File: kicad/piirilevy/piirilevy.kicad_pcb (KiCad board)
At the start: 2 copper layers, 57 parts, among them SW1 SW_SPST, SW2 SW_Push, SW3 SW_Push, SW4 SW_Push, U1 LM324, U2 uA7805, U3 ATmega328P, U4 MAX5033B, U5 MCP3202, U6 47C16, Y1 16MHz

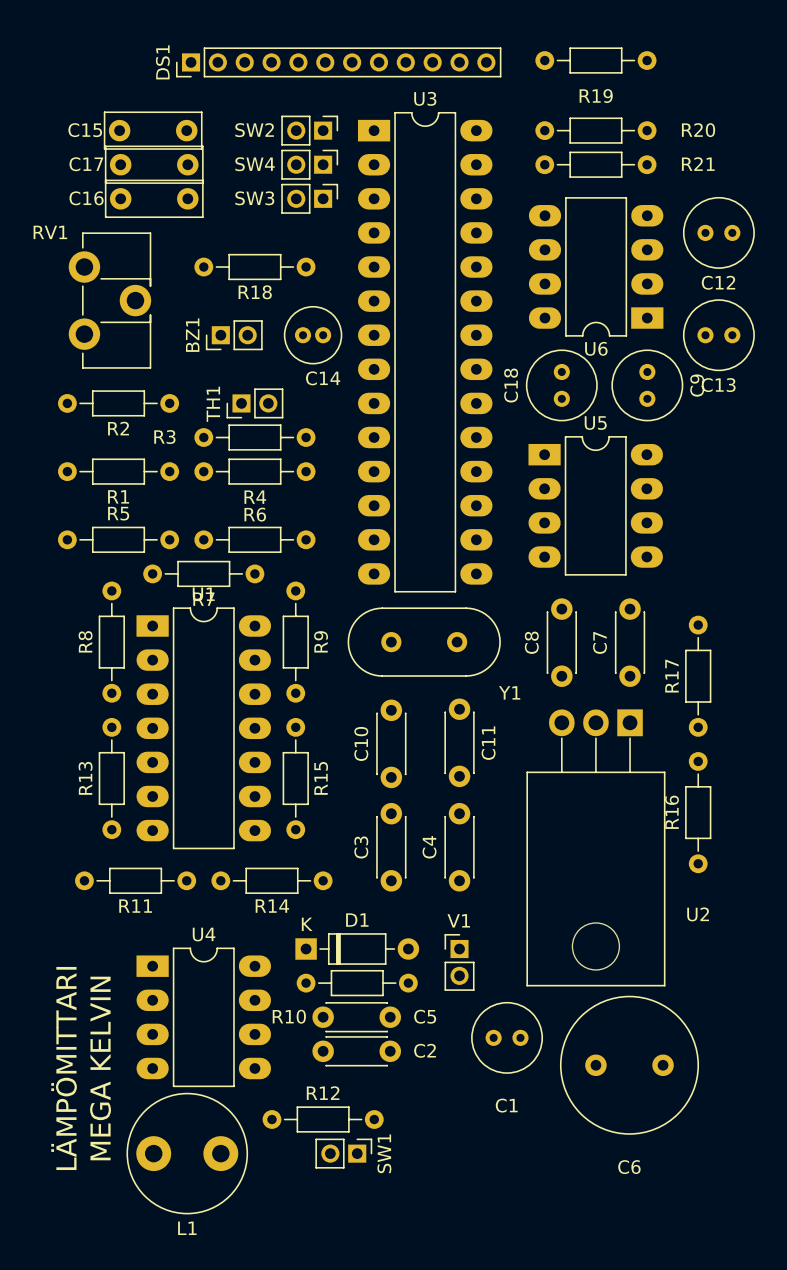
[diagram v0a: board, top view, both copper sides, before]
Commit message: Testausreititys piirilevylle.
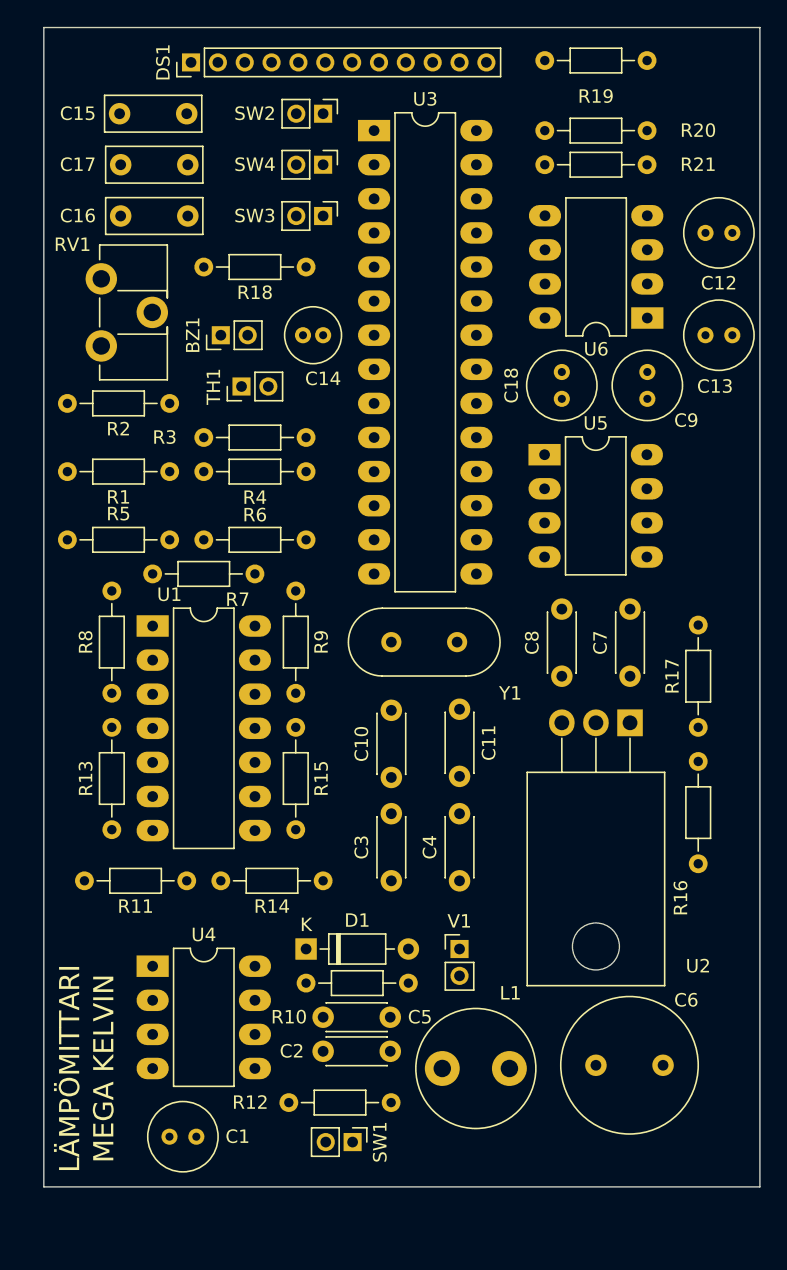
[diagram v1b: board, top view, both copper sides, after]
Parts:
- moved C1 25.2 mm to (121.9, 114.3)
- moved L1 17.7 mm to (142.2, 109.2), turned to 0 degrees
- moved R12 1.78 mm to (130.8, 111.8)
- moved RV1 1.53 mm to (116.8, 50.4)
- moved C16 1.28 mm to (118.3, 45.7)
- moved SW3 1.28 mm to (133.4, 45.7)
- moved C15 1.26 mm to (118.2, 38.1)
- moved SW2 1.26 mm to (133.4, 38.1)
- moved TH1 1.26 mm to (127.3, 58.4)
- moved SW1 0.93 mm to (135.6, 114.7)
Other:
- board outline added: 53.3 x 86.4 mm

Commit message: kicad muutokset
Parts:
- added D2: 1N4148, Diode_THT:D_DO-35_SOD27_P7.62mm_Horizontal, F.Cu at (160.0, 52.1)
- added H1: MountingHole_2.1mm, MountingHole:MountingHole_2.1mm, F.Cu at (114.3, 25.4)
- added H2: MountingHole_2.1mm, MountingHole:MountingHole_2.1mm, F.Cu at (162.6, 25.4)
- added H3: MountingHole_2.1mm, MountingHole:MountingHole_2.1mm, F.Cu at (162.6, 116.8)
- added H4: MountingHole_2.1mm, MountingHole:MountingHole_2.1mm, F.Cu at (114.3, 116.8)
- added J1: AVR-ISP, Connector_PinHeader_2.54mm:PinHeader_2x03_P2.54mm_Vertical, F.Cu at (154.9, 55.9)
- BZ1, SW1, SW2, SW3, SW4, TH1: footprint Connector_PinHeader_2.00mm:PinHeader_1x02_P2.00mm_Vertical -> Connector_PinHeader_2.54mm:PinHeader_1x02_P2.54mm_Vertical
- DS1: footprint Connector_PinHeader_2.00mm:PinHeader_1x12_P2.00mm_Vertical -> Connector_PinHeader_2.54mm:PinHeader_1x12_P2.54mm_Vertical
- RV1: footprint Potentiometer_THT:Potentiometer_ACP_CA9-H3,8_Horizontal -> Potentiometer_THT:Potentiometer_ACP_CA6-H2,5_Horizontal
- moved R19 40.8 mm to (116.8, 30.5), turned to 0 degrees
- moved R20 30.5 mm to (128.3, 30.5), turned to 0 degrees
- moved C13 24.7 mm to (158.4, 30.5)
- moved C12 20.1 mm to (152.4, 30.5)
- moved C5 16.6 mm to (116.8, 104.1), turned to 90 degrees
- moved C2 16.6 mm to (116.8, 106.7), turned to -90 degrees
- moved R21 16.2 mm to (146.1, 30.5)
- moved C1 13.8 mm to (133.6, 106.9)
- moved R12 10.2 mm to (120.7, 111.8)
- moved C9 9.29 mm to (155.5, 48.3)
- moved C18 9.17 mm to (149.9, 48.3)
- moved U6 8.97 mm to (158.8, 44.4)
- moved DS1 5.22 mm to (118.3, 34.2)
- moved SW1 2.94 mm to (135.6, 111.8)
- moved SW2 1.28 mm to (132.1, 38.1)
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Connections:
- net SW_3 renamed RESET
- U1 pad 11: (no net) -> GND
- U1 pad 4: (no net) -> VCC
- U3 pad 7: VCC -> ISP_VCC
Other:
- board size 53.3 x 86.4 mm -> 53.3 x 96.5 mm
- board text removed: "LÄMPÖMITTARI"
- board text removed: "MEGA KELVIN"

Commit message: Torstain muutokset.
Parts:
- C1: footprint Capacitor_THT:C_Radial_D5.0mm_H7.0mm_P2.00mm -> Capacitor_THT:C_Radial_D6.3mm_H5.0mm_P2.50mm
- C12, C13: footprint Capacitor_THT:C_Radial_D5.0mm_H7.0mm_P2.00mm -> Capacitor_THT:C_Radial_D5.0mm_H5.0mm_P2.00mm
- C14: footprint Capacitor_THT:C_Radial_D4.0mm_H5.0mm_P1.50mm -> Capacitor_THT:C_Radial_D5.0mm_H5.0mm_P2.00mm
- C6: value 1m -> 330u; footprint Capacitor_THT:C_Radial_D10.0mm_H16.0mm_P5.00mm -> Capacitor_THT:C_Radial_D8.0mm_H7.0mm_P3.50mm
- C7: value 10n -> 330n
- C8: value 10n -> 100n
- L1: footprint Inductor_THT:L_Radial_D8.7mm_P5.00mm_Fastron_07HCP -> Capacitor_THT:C_Radial_D8.0mm_H7.0mm_P3.50mm
- R16: value 5M -> 820k
- R17: value 1M -> 180k
- RV1: footprint Potentiometer_THT:Potentiometer_ACP_CA6-H2,5_Horizontal -> Potentiometer_THT:Potentiometer_Vishay_T73YP_Vertical
- U2: value uA7805 -> LM7805CV
- moved RV1 4.74 mm to (117.4, 55.1)
- moved SW1 1.20 mm to (135.6, 113.0)
- moved BZ1 1.00 mm to (124.7, 54.6)
- moved U2 0.91 mm to (155.5, 84.0)
- moved C14 0.90 mm to (133.4, 53.7)
- moved C1 0.60 mm to (133.6, 107.5)
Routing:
- net LCD_RS: track 0.00 -> 45.8 mm
- net VAHVISTIN_LÄHTÖ: track 0.00 -> 43.4 mm
- net LCD_CL: track 0.00 -> 41.8 mm
- net V_KÄYTTÖ: track 0.00 -> 41.1 mm
- net RESET: track 0.00 -> 39.5 mm
- net SPI_MISO: track 0.00 -> 30.9 mm
- net Net-(C5-Pad1): track 0.00 -> 30.7 mm
- net LCD_AN: track 0.00 -> 30.6 mm
- net Net-(R2-Pad1): track 0.00 -> 30.0 mm
- net ISP_VCC: track 0.00 -> 28.6 mm
- net Net-(R10-Pad2): track 0.00 -> 28.4 mm
- net Net-(C3-Pad1): track 0.00 -> 27.7 mm
- net Net-(R11-Pad2): track 0.00 -> 27.3 mm
- net XTAL_1: track 0.00 -> 26.3 mm
- net SPI_MOSI: track 0.00 -> 26.2 mm
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- added copper zone on B.Cu, net GND
- added copper zone on F.Cu, net VCC

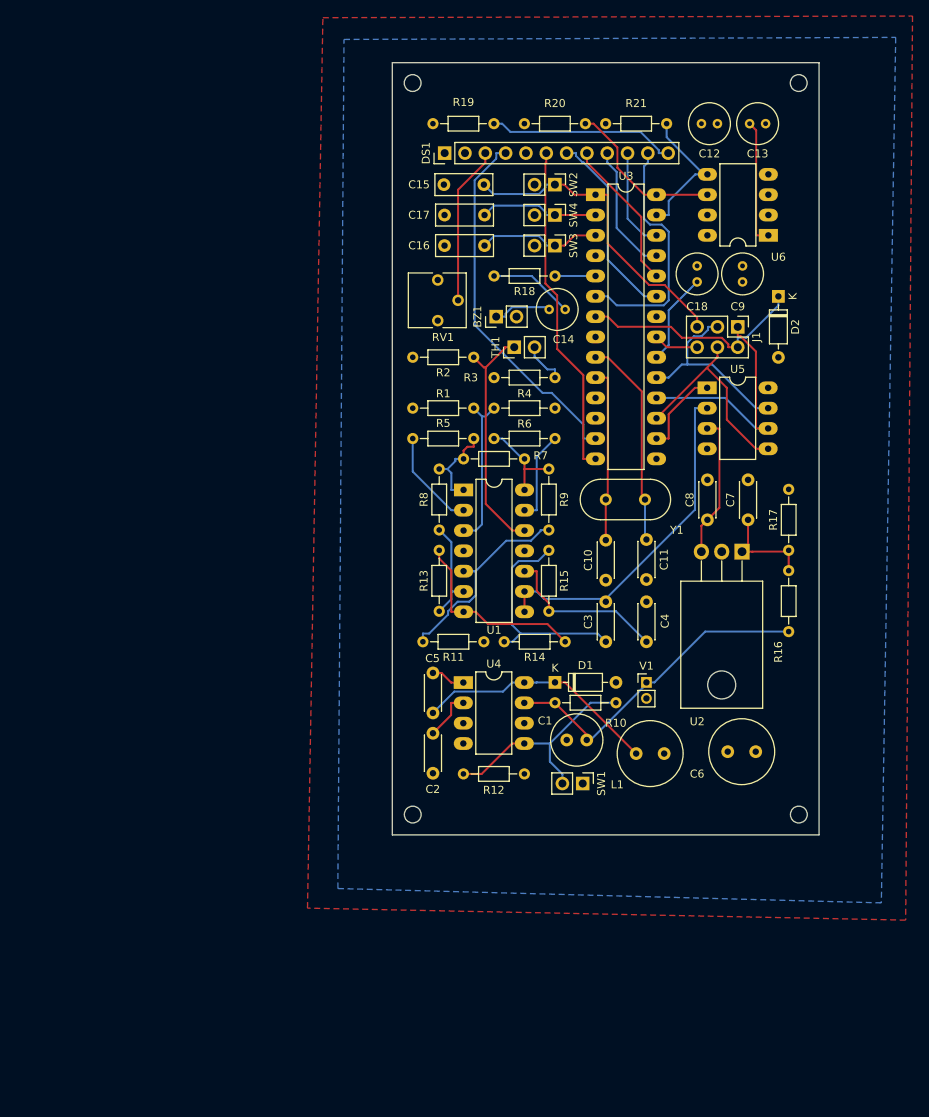
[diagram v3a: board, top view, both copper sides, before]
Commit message: Korjaukset piirilevyyn + CNC tiedostot ja kuvat.
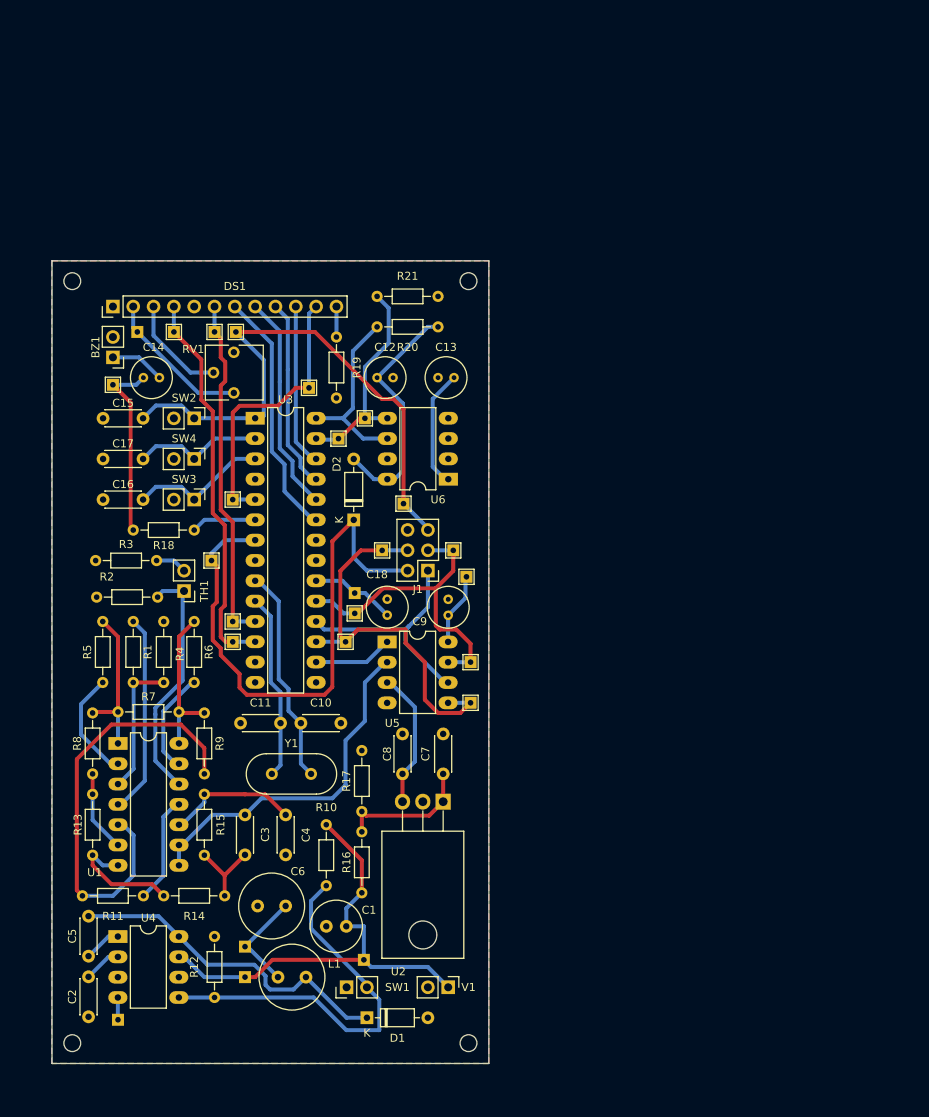
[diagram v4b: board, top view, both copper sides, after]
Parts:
- removed H2: MountingHole_2.1mm, MountingHole:MountingHole_2.1mm
- added ?: , , F.Cu at (93.3, 137.2)
- added ?: , , F.Cu at (79.9, 56.5)
- added ?: , , F.Cu at (108.2, 135.0)
- added ?: , , F.Cu at (77.5, 142.5)
- added ?: , , F.Cu at (93.3, 133.3)
- added ?: , , F.Cu at (107.1, 89.2)
- added H1: MountingHole_2.1mm, MountingHole:MountingHole_2.1mm, F.Cu at (71.8, 50.2)
- added REF**: TestPoint_THTPad_1.5x1.5mm_Drill0.7mm, TestPoint:TestPoint_THTPad_1.5x1.5mm_Drill0.7mm, F.Cu at (119.4, 83.8)
- added REF**: TestPoint_THTPad_1.5x1.5mm_Drill0.7mm, TestPoint:TestPoint_THTPad_1.5x1.5mm_Drill0.7mm, F.Cu at (108.3, 67.3)
- added REF**: TestPoint_THTPad_1.5x1.5mm_Drill0.7mm, TestPoint:TestPoint_THTPad_1.5x1.5mm_Drill0.7mm, F.Cu at (107.1, 91.7)
- added REF**: TestPoint_THTPad_1.5x1.5mm_Drill0.7mm, TestPoint:TestPoint_THTPad_1.5x1.5mm_Drill0.7mm, F.Cu at (92.2, 56.5)
- added REF**: TestPoint_THTPad_1.5x1.5mm_Drill0.7mm, TestPoint:TestPoint_THTPad_1.5x1.5mm_Drill0.7mm, F.Cu at (101.3, 63.5)
- added REF**: TestPoint_THTPad_1.5x1.5mm_Drill0.7mm, TestPoint:TestPoint_THTPad_1.5x1.5mm_Drill0.7mm, F.Cu at (110.5, 83.8)
- added REF**: TestPoint_THTPad_1.5x1.5mm_Drill0.7mm, TestPoint:TestPoint_THTPad_1.5x1.5mm_Drill0.7mm, F.Cu at (105.9, 95.2)
- added REF**: TestPoint_THTPad_1.5x1.5mm_Drill0.7mm, TestPoint:TestPoint_THTPad_1.5x1.5mm_Drill0.7mm, F.Cu at (121.5, 102.9)
- added REF**: TestPoint_THTPad_1.5x1.5mm_Drill0.7mm, TestPoint:TestPoint_THTPad_1.5x1.5mm_Drill0.7mm, F.Cu at (91.8, 95.2)
- added REF**: TestPoint_THTPad_1.5x1.5mm_Drill0.7mm, TestPoint:TestPoint_THTPad_1.5x1.5mm_Drill0.7mm, F.Cu at (84.5, 56.5)
- added REF**: TestPoint_THTPad_1.5x1.5mm_Drill0.7mm, TestPoint:TestPoint_THTPad_1.5x1.5mm_Drill0.7mm, F.Cu at (89.2, 85.1)
- added REF**: TestPoint_THTPad_1.5x1.5mm_Drill0.7mm, TestPoint:TestPoint_THTPad_1.5x1.5mm_Drill0.7mm, F.Cu at (76.8, 63.1)
- added REF**: TestPoint_THTPad_1.5x1.5mm_Drill0.7mm, TestPoint:TestPoint_THTPad_1.5x1.5mm_Drill0.7mm, F.Cu at (91.8, 77.5)
- added REF**: TestPoint_THTPad_1.5x1.5mm_Drill0.7mm, TestPoint:TestPoint_THTPad_1.5x1.5mm_Drill0.7mm, F.Cu at (91.8, 92.7)
- added REF**: TestPoint_THTPad_1.5x1.5mm_Drill0.7mm, TestPoint:TestPoint_THTPad_1.5x1.5mm_Drill0.7mm, F.Cu at (121.0, 87.1)
- added REF**: TestPoint_THTPad_1.5x1.5mm_Drill0.7mm, TestPoint:TestPoint_THTPad_1.5x1.5mm_Drill0.7mm, F.Cu at (89.5, 56.5)
- added REF**: TestPoint_THTPad_1.5x1.5mm_Drill0.7mm, TestPoint:TestPoint_THTPad_1.5x1.5mm_Drill0.7mm, F.Cu at (113.2, 78.0)
- added REF**: TestPoint_THTPad_1.5x1.5mm_Drill0.7mm, TestPoint:TestPoint_THTPad_1.5x1.5mm_Drill0.7mm, F.Cu at (105.0, 69.8)
- added REF**: TestPoint_THTPad_1.5x1.5mm_Drill0.7mm, TestPoint:TestPoint_THTPad_1.5x1.5mm_Drill0.7mm, F.Cu at (121.5, 97.8)
- C15, C16, C17: footprint Capacitor_THT:C_Rect_L7.0mm_W2.5mm_P5.00mm -> Capacitor_THT:C_Disc_D4.3mm_W1.9mm_P5.00mm
- R10, R12: value 1k -> 10k
- V1: footprint Connector_PinHeader_2.00mm:PinHeader_1x02_P2.00mm_Vertical -> Connector_PinHeader_2.54mm:PinHeader_1x02_P2.54mm_Vertical
- moved H1 120.2 mm to (121.3, 145.4)
- moved H3 95.2 mm to (71.8, 145.4)
- moved H4 67.0 mm to (121.3, 50.2)
- moved R16 62.6 mm to (108.0, 126.6)
- moved R17 62.6 mm to (108.0, 116.5)
- moved D2 60.0 mm to (106.9, 80.0), turned to 90 degrees
- moved R14 59.4 mm to (83.2, 127.0), turned to 0 degrees
- moved C6 58.5 mm to (98.4, 128.3), turned to 180 degrees
- moved R15 57.5 mm to (88.3, 121.9), turned to 90 degrees
- moved C9 57.1 mm to (118.7, 91.9), turned to 90 degrees
- moved C18 56.9 mm to (111.1, 89.9)
- moved R18 55.2 mm to (87.0, 81.3)
- moved SW3 55.1 mm to (87.0, 77.5)
- moved R3 54.8 mm to (74.7, 85.1)
- moved R1 54.7 mm to (79.4, 100.3), turned to 90 degrees
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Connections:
- U3 pad 10: XTAL_2 -> XTAL_1
- U3 pad 11: unconnected-(U3-Pad11) -> LCD_CL
- U3 pad 12: unconnected-(U3-Pad12) -> LCD_RS
- U3 pad 13: LCD_RS -> unconnected-(U3-Pad13)
- U3 pad 14: LCD_CL -> unconnected-(U3-Pad14)
- U3 pad 5: BUZZER -> LCD_AN
- U3 pad 6: LCD_AN -> BUZZER
- U3 pad 9: XTAL_1 -> XTAL_2
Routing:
- net VCC: track 11.5 -> 110.1 mm
- net ISP_VCC: track 28.6 -> 71.3 mm
- net RESET: track 39.5 -> 69.8 mm
- net Net-(R11-Pad2): track 27.3 -> 54.5 mm
- net SPI_MOSI: track 26.2 -> 49.9 mm
- net Net-(R10-Pad2): track 28.4 -> 49.1 mm
- net Net-(DS1-Pad12): track 23.5 -> 3.81 mm
- net Net-(C3-Pad1): track 27.7 -> 9.76 mm
- net V_KÄYTTÖ: track 41.1 -> 58.8 mm
- net SPI_SCK: track 24.4 -> 40.8 mm
- net Net-(C14-Pad1): track 10.6 -> 23.4 mm
- net Net-(C5-Pad1): track 30.7 -> 42.0 mm
- net I2C_SDA: track 17.8 -> 27.1 mm
- net Net-(R13-Pad2): track 24.1 -> 15.4 mm
- net LCD_D5: track 19.0 -> 27.3 mm
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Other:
- board size 53.3 x 96.5 mm -> 54.6 x 100.3 mm

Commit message: 3D kuva piirilevystä.
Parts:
- removed ? (x6): , 
- added REF**: TestPoint_THTPad_1.5x1.5mm_Drill0.7mm, TestPoint:TestPoint_THTPad_1.5x1.5mm_Drill0.7mm, F.Cu at (77.5, 142.5)
- added REF**: TestPoint_THTPad_1.5x1.5mm_Drill0.7mm, TestPoint:TestPoint_THTPad_1.5x1.5mm_Drill0.7mm, F.Cu at (108.2, 135.0)
- added REF**: TestPoint_THTPad_1.5x1.5mm_Drill0.7mm, TestPoint:TestPoint_THTPad_1.5x1.5mm_Drill0.7mm, F.Cu at (79.9, 56.5)
- added REF**: TestPoint_THTPad_1.5x1.5mm_Drill0.7mm, TestPoint:TestPoint_THTPad_1.5x1.5mm_Drill0.7mm, F.Cu at (93.3, 133.3)
- added REF**: TestPoint_THTPad_1.5x1.5mm_Drill0.7mm, TestPoint:TestPoint_THTPad_1.5x1.5mm_Drill0.7mm, F.Cu at (93.3, 137.2)
- added REF**: TestPoint_THTPad_1.5x1.5mm_Drill0.7mm, TestPoint:TestPoint_THTPad_1.5x1.5mm_Drill0.7mm, F.Cu at (107.1, 89.2)
